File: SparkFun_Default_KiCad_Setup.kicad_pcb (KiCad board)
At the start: 4 copper layers, 50.8 x 50.8 mm, 12 parts

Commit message: Add copper weight
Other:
- board text added: "Copper Weight: 1oz"
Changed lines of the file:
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@@
+    (effects (font (size 2 2) (thickness 0.15)) (justify left bottom))
+  )
+  (gr_text "Copper Weight: 1oz" (at 166.37 128.27) (layer "F.Fab")
     (effects (font (size 2 2) (thickness 0.15)) (justify left bottom))
   )

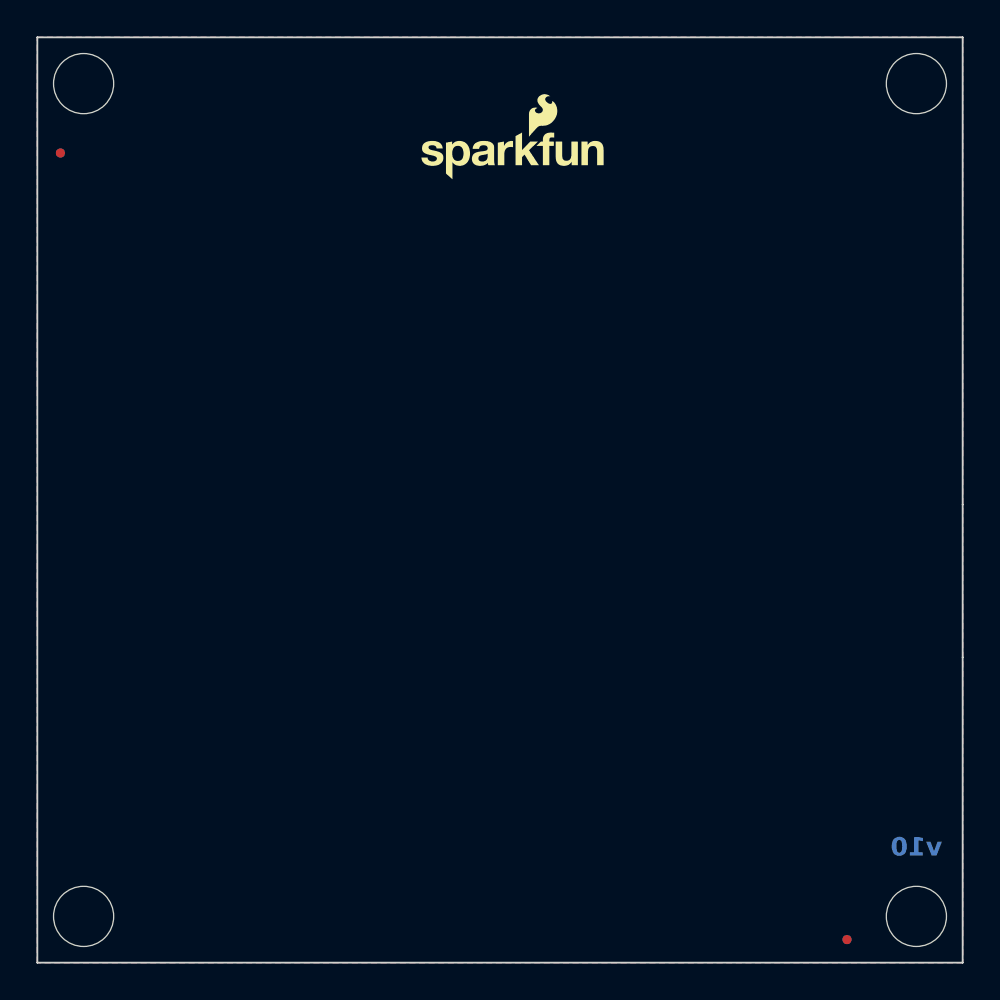
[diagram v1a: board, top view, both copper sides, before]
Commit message: Update fiducial symbol
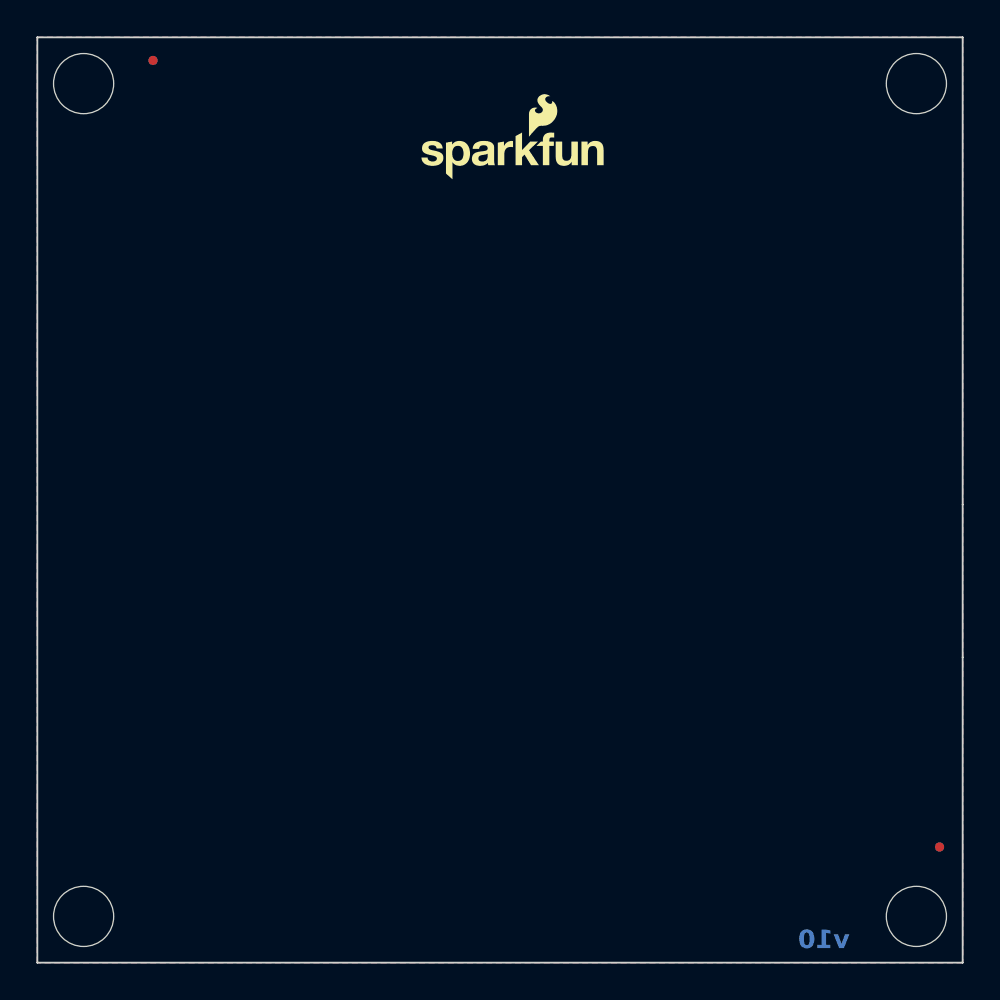
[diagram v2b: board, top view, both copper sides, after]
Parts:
- FID1: value Fiducial_0.5 -> Fiducial_0.5mm; moved to F.Cu
- FID2, FID4: value Fiducial_0.5 -> Fiducial_0.5mm
- FID3: value Fiducial_0.5 -> Fiducial_0.5mm; moved to B.Cu
- U1: renamed from U7; footprint SparkFun-Aesthetic:Ordering_Instructions -> SparkFun-Aesthetic:ORDERING_INSTRUCTIONS
- moved FID1 61.5 mm to (108.0, 102.9), turned to 0 degrees
- moved FID2 61.5 mm to (151.1, 146.1)
- moved FID3 7.18 mm to (108.0, 102.9), turned to 180 degrees
- moved FID4 7.18 mm to (151.1, 146.1)
- renumbered G1 to G3, ST3 to ST1, ST4 to ST2, ST1 to ST3, ST2 to ST4
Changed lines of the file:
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@@
   )
   (net 0 "")
-  (footprint "SparkFun-Aesthetic:Fiducial_0.5mm_Mask1mm" (layer "F.Cu")
-    (at 102.87 107.95)
-    (descr "Circular Fiducial, 0.5mm bare copper, 1mm soldermask opening (Level C)")
-    (tags "fiducial")
-    (property "Sheetfile" "SparkFun_Default_KiCad_Setup.kicad_sch")
-    (property "Sheetname" "")
-    (property "ki_description" "Fiducial Marker")
-    (property "ki_keywords" "fiducial marker")
-    (attr smd)
-    (fp_text reference "FID3" (at 0 -1.5) (layer "F.Fab")
-        (effects (font (size 0.5 0.5) (thickness 0.1)))
-    )
-    (fp_text value "Fiducial_0.5" (at 0 1.5) (layer "F.Fab")
-        (effects (font (size 0.5 0.5) (thickness 0.1)))
-    )
-    (fp_circle (center 0 0) (end 0.75 0)
-      (stroke (width 0.05) (type solid)) (fill none) (layer "F.CrtYd"))
-    (fp_circle (center 0 0) (end 0.5 0)
-      (stroke (width 0.1) (type solid)) (fill none) (layer "F.Fab"))
-    (pad "" smd circle (at 0 0) (size 0.5 0.5) (layers "F.Cu" "F.Mask")
-      (solder_mask_margin 0.25) (clearance 0.25))
-  )
   (footprint "SparkFun-Hardware:STAND-OFF" (layer "F.Cu")
     (at 149.86 149.86)
@@
     (property "ki_description" "Drill holes for mechanically mounting via screws, standoffs, etc.")
     (property "ki_keywords" "#4 screw stand off")
-    (fp_text reference "ST2" (at 0 -2.032) (layer "F.Fab")
+    (fp_text reference "ST4" (at 0 -2.032) (layer "F.Fab")
         (effects (font (size 0.5 0.5) (thickness 0.1)) (justify bottom))
     )
@@
     (pad "" np_thru_hole circle (at 0 0) (size 3.302 3.302) (drill 3.302) (layers "F&B.Cu" "*.Mask"))
   )
-  (footprint "SparkFun-Aesthetic:Ordering_Instructions" (layer "F.Cu")
+  (footprint "SparkFun-Aesthetic:ORDERING_INSTRUCTIONS" (layer "F.Cu")
     (at 165.1 101.6)
     (property "Sheetfile" "SparkFun_Default_KiCad_Setup.kicad_sch")
     (property "Sheetname" "")
-    (fp_text reference "U7" (at 2.54 -1.27) (layer "F.Fab") hide
+    (fp_text reference "U1" (at 2.54 -1.27) (layer "F.Fab") hide
         (effects (font (size 1.27 1.27) (thickness 0.15)))
     )
@@
         (effects (font (size 1.27 1.27) (thickness 0.15)))
     )
-    (fp_text user "Ordering Instructions:" (at 1.27 1.27) (layer "Cmts.User")
+    (fp_text user "Ordering Instructions:" (at 1.27 1.27) (layer "User.1")
         (effects (font (size 2.5908 2.5908) (thickness 0.4572)) (justify left top))
     )
     (fp_line (start 0 4.445) (end 63.5 4.445)
-      (stroke (width 0.2032) (type solid)) (layer "Cmts.User"))
+      (stroke (width 0.2032) (type solid)) (layer "User.1"))
     (fp_rect (start 0 0) (end 63.5 50.8)
-      (stroke (width 0.2) (type default)) (fill none) (layer "Cmts.User"))
+      (stroke (width 0.2) (type default)) (fill none) (layer "User.1"))
   )
   (footprint "SparkFun-Aesthetic:Fiducial_0.5mm_Mask1mm" (layer "F.Cu")
-    (at 146.05 151.13)
+    (at 151.13 146.05)
     (descr "Circular Fiducial, 0.5mm bare copper, 1mm soldermask opening (Level C)")
     (tags "fiducial")
@@
         (effects (font (size 0.5 0.5) (thickness 0.1)))
     )
-    (fp_text value "Fiducial_0.5" (at 0 1.5) (layer "F.Fab")
+    (fp_text value "Fiducial_0.5mm" (at 0 1.5) (layer "F.Fab")
+        (effects (font (size 0.5 0.5) (thickness 0.1)))
+    )
+    (fp_circle (center 0 0) (end 0.75 0)
+      (stroke (width 0.05) (type solid)) (fill none) (layer "F.CrtYd"))
+    (fp_circle (center 0 0) (end 0.5 0)
+      (stroke (width 0.1) (type solid)) (fill none) (layer "F.Fab"))
+    (pad "" smd circle (at 0 0) (size 0.5 0.5) (layers "F.Cu" "F.Mask")
+      (solder_mask_margin 0.25) (clearance 0.25))
+  )
+  (footprint "SparkFun-Aesthetic:Fiducial_0.5mm_Mask1mm" (layer "F.Cu")
+    (at 107.95 102.87)
+    (descr "Circular Fiducial, 0.5mm bare copper, 1mm soldermask opening (Level C)")
+    (tags "fiducial")
+    (property "Sheetfile" "SparkFun_Default_KiCad_Setup.kicad_sch")
+    (property "Sheetname" "")
+    (property "ki_description" "Fiducial Marker")
+    (property "ki_keywords" "fiducial marker")
+    (attr smd)
+    (fp_text reference "FID1" (at 0 -1.5) (layer "F.Fab")
+        (effects (font (size 0.5 0.5) (thickness 0.1)))
+    )
+    (fp_text value "Fiducial_0.5mm" (at 0 1.5) (layer "F.Fab")
         (effects (font (size 0.5 0.5) (thickness 0.1)))
     )
@@
     (property "ki_description" "Drill holes for mechanically mounting via screws, standoffs, etc.")
     (property "ki_keywords" "#4 screw stand off")
-    (fp_text reference "ST1" (at 0 -2.032) (layer "F.Fab")
+    (fp_text reference "ST3" (at 0 -2.032) (layer "F.Fab")
         (effects (font (size 0.5 0.5) (thickness 0.1)) (justify bottom))
     )
@@
     (property "ki_description" "Drill holes for mechanically mounting via screws, standoffs, etc.")
     (property "ki_keywords" "#4 screw stand off")
-    (fp_text reference "ST3" (at 0 -2.032) (layer "F.Fab")
+    (fp_text reference "ST1" (at 0 -2.032) (layer "F.Fab")
         (effects (font (size 0.5 0.5) (thickness 0.1)) (justify bottom))
     )
@@
     (property "ki_keywords" "Open Source Hardware Logo")
     (attr exclude_from_bom)
-    (fp_text reference "G1" (at 0 -5.08) (layer "F.Fab") hide
+    (fp_text reference "G3" (at 0 -5.08) (layer "F.Fab") hide
         (effects (font (size 1.27 1.27) (thickness 0.15)))
     )
@@
     (property "ki_description" "Drill holes for mechanically mounting via screws, standoffs, etc.")
     (property "ki_keywords" "#4 screw stand off")
-    (fp_text reference "ST4" (at 0 -2.032) (layer "F.Fab")
+    (fp_text reference "ST2" (at 0 -2.032) (layer "F.Fab")
         (effects (font (size 0.5 0.5) (thickness 0.1)) (justify bottom))
     )
@@
   )
   (footprint "SparkFun-Aesthetic:Fiducial_0.5mm_Mask1mm" (layer "B.Cu")
-    (at 102.87 107.95 180)
+    (at 107.95 102.87 180)
     (descr "Circular Fiducial, 0.5mm bare copper, 1mm soldermask opening (Level C)")
     (tags "fiducial")
@@
     (property "ki_keywords" "fiducial marker")
     (attr smd)
-    (fp_text reference "FID2" (at 0 1.5) (layer "B.Fab")
+    (fp_text reference "FID3" (at 0 1.5) (layer "B.Fab")
         (effects (font (size 0.5 0.5) (thickness 0.1)) (justify mirror))
     )
-    (fp_text value "Fiducial_0.5" (at 0 -1.5) (layer "B.Fab")
+    (fp_text value "Fiducial_0.5mm" (at 0 -1.5) (layer "B.Fab")
         (effects (font (size 0.5 0.5) (thickness 0.1)) (justify mirror))
     )
@@
   )
   (footprint "SparkFun-Aesthetic:Fiducial_0.5mm_Mask1mm" (layer "B.Cu")
-    (at 146.05 151.13 180)
+    (at 151.13 146.05 180)
     (descr "Circular Fiducial, 0.5mm bare copper, 1mm soldermask opening (Level C)")
     (tags "fiducial")
@@
     (property "ki_keywords" "fiducial marker")
     (attr smd)
-    (fp_text reference "FID1" (at 0 1.5) (layer "B.Fab")
+    (fp_text reference "FID2" (at 0 1.5) (layer "B.Fab")
         (effects (font (size 0.5 0.5) (thickness 0.1)) (justify mirror))
     )
-    (fp_text value "Fiducial_0.5" (at 0 -1.5) (layer "B.Fab")
+    (fp_text value "Fiducial_0.5mm" (at 0 -1.5) (layer "B.Fab")
         (effects (font (size 0.5 0.5) (thickness 0.1)) (justify mirror))
     )
@@
     )
     (stroke (width 0.1) (type solid)) (fill none) (layer "Edge.Cuts"))
-  (gr_text "v10" (at 149.86 146.05) (layer "B.Cu" knockout)
+  (gr_text "v10" (at 144.78 151.13) (layer "B.Cu" knockout)
     (effects (font (size 1.016 1.016) (thickness 0.254) bold) (justify mirror))
   )

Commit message: Add inner/outer copper weights
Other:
- board text added: "Inner Copper Weight: 0.5oz"
- board text added: "Outer Copper Weight: 1oz"
- board text removed: "Copper Weight: 1oz"
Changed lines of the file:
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@@
+    (effects (font (size 2 2) (thickness 0.15)) (justify left bottom))
+  )
+  (gr_text "Inner Copper Weight: 0.5oz" (at 166.37 131.1275) (layer "F.Fab")
     (effects (font (size 2 2) (thickness 0.15)) (justify left bottom))
   )
@@
     (effects (font (size 2 2) (thickness 0.15)) (justify left bottom))
   )
-  (gr_text "Copper Weight: 1oz" (at 166.37 128.27) (layer "F.Fab")
+  (gr_text "Outer Copper Weight: 1oz" (at 166.37 128.27) (layer "F.Fab")
     (effects (font (size 2 2) (thickness 0.15)) (justify left bottom))
   )
